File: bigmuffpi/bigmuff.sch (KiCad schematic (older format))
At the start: 62 parts, among them J1 PWR JACK, J2 INPUT, J3 OUTPUT, Q1 BC239, Q2 BC239, Q3 BC239, Q4 BC239, SW1 POWER

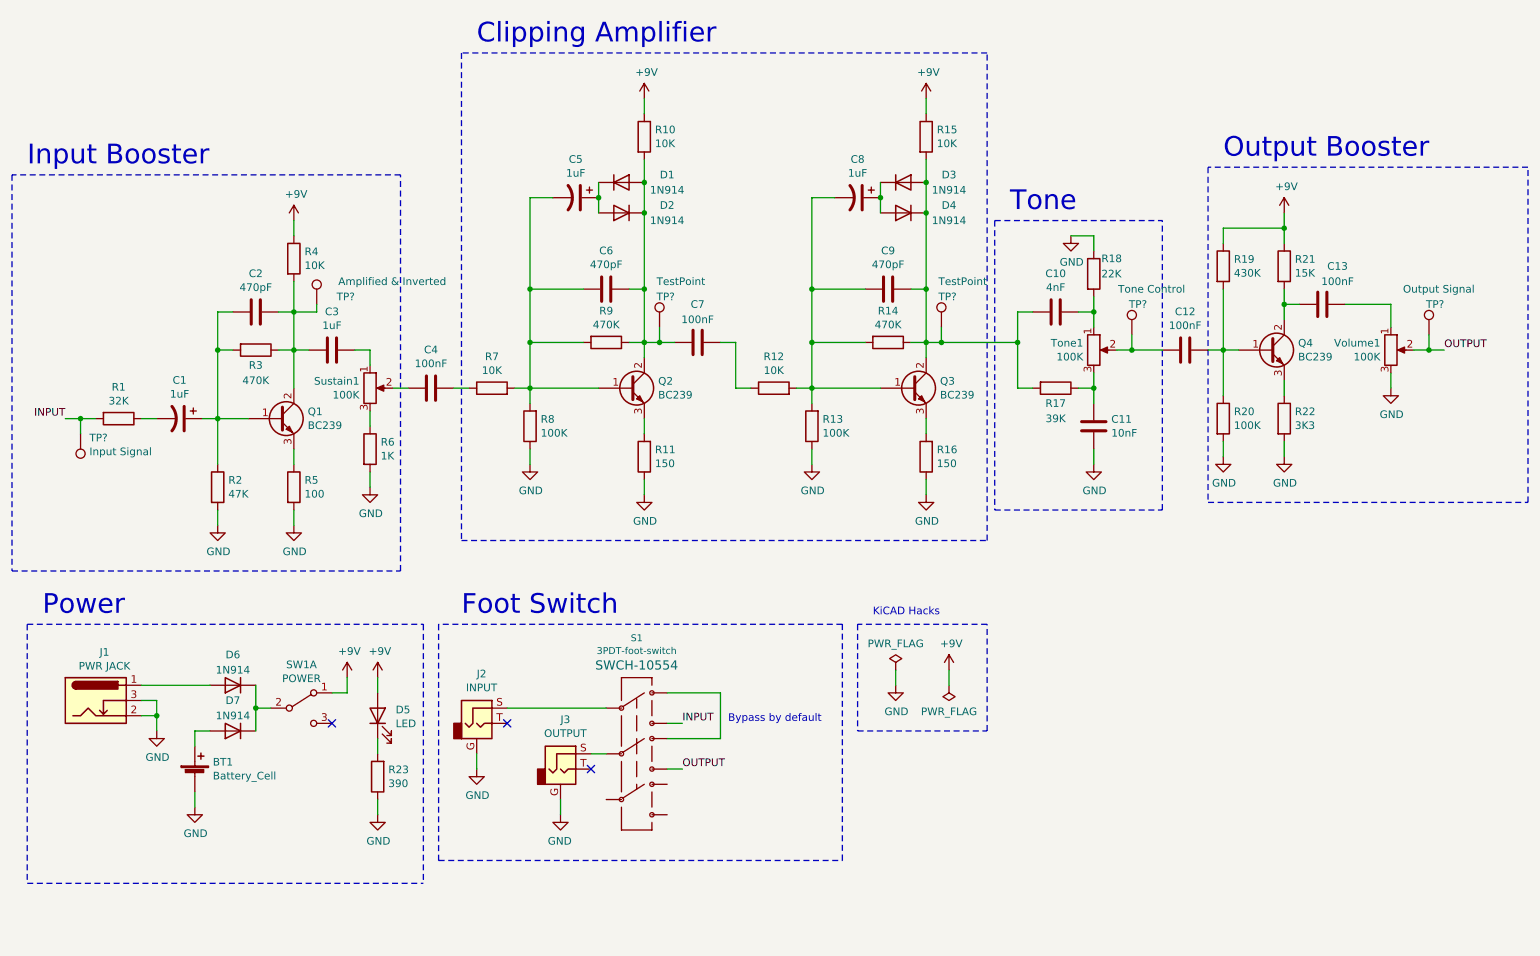
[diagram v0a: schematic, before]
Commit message: add: not connected to switch
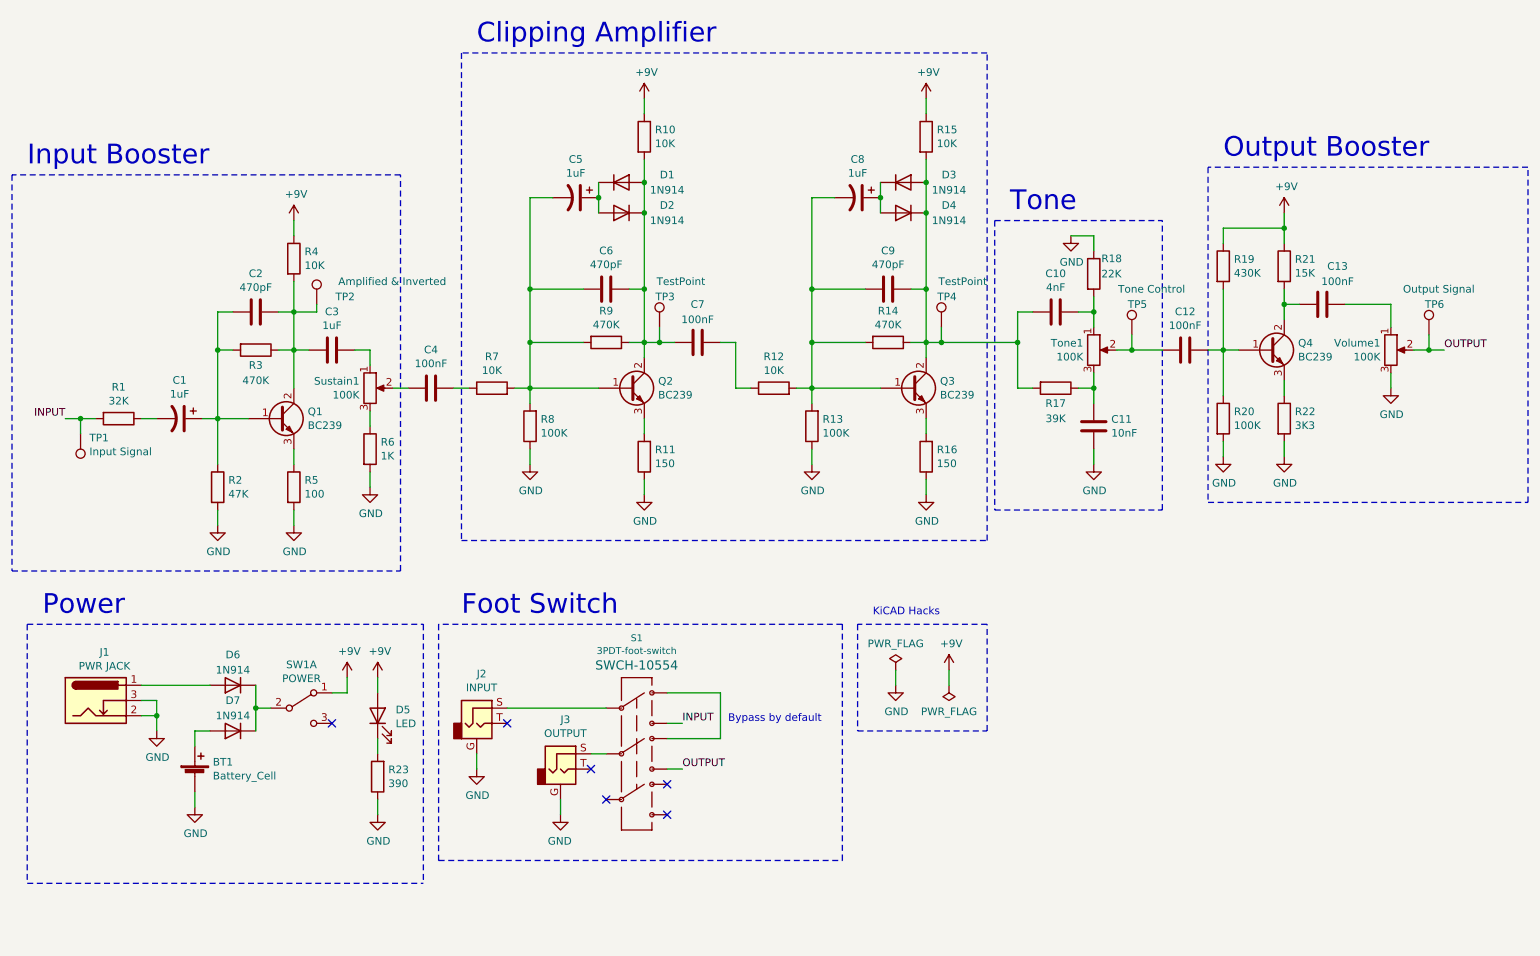
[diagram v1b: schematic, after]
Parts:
- gave numbers to parts that had none: 6
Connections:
- no-connect marks 3 -> 6
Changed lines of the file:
@@
 	1200 5350 3800 5350
 $Comp
-L Connector:TestPoint TP?
+L Connector:TestPoint TP1
 U 1 1 5F1F2FF8
 P 1550 4100
-F 0 "TP?" H 1492 4126 50  0000 R CNN
+F 0 "TP1" H 1492 4126 50  0000 R CNN
 F 1 "Input Signal" H 1492 4217 50  0000 R CNN
 F 2 "" H 1750 4100 50  0001 C CNN
@@
 Connection ~ 1550 4000
 $Comp
-L Connector:TestPoint TP?
+L Connector:TestPoint TP3
 U 1 1 5F208773
 P 5350 3400
-F 0 "TP?" H 5450 3600 50  0000 R CNN
+F 0 "TP3" H 5450 3600 50  0000 R CNN
 F 1 "TestPoint" H 5650 3700 50  0000 R CNN
 F 2 "" H 5550 3400 50  0001 C CNN
@@
 	5350 3500 5450 3500
 $Comp
-L Connector:TestPoint TP?
+L Connector:TestPoint TP4
 U 1 1 5F22B391
 P 7200 3400
-F 0 "TP?" H 7300 3600 50  0000 R CNN
+F 0 "TP4" H 7300 3600 50  0000 R CNN
 F 1 "TestPoint" H 7500 3700 50  0000 R CNN
 F 2 "" H 7400 3400 50  0001 C CNN
@@
 	7200 3500 7700 3500
 $Comp
-L Connector:TestPoint TP?
+L Connector:TestPoint TP6
 U 1 1 5F2380CB
 P 10400 3450
-F 0 "TP?" H 10500 3650 50  0000 R CNN
+F 0 "TP6" H 10500 3650 50  0000 R CNN
 F 1 "Output Signal" H 10700 3750 50  0000 R CNN
 F 2 "" H 10600 3450 50  0001 C CNN
@@
 Connection ~ 10400 3550
 $Comp
-L Connector:TestPoint TP?
+L Connector:TestPoint TP5
 U 1 1 5F24FCF1
 P 8450 3450
-F 0 "TP?" H 8550 3650 50  0000 R CNN
+F 0 "TP5" H 8550 3650 50  0000 R CNN
 F 1 "Tone Control" H 8800 3750 50  0000 R CNN
 F 2 "" H 8650 3450 50  0001 C CNN
@@
 	2950 3300 3100 3300
 $Comp
-L Connector:TestPoint TP?
+L Connector:TestPoint TP2
 U 1 1 5F2936BD
 P 3100 3250
-F 0 "TP?" H 3350 3300 50  0000 R CNN
+F 0 "TP2" H 3350 3300 50  0000 R CNN
 F 1 "Amplified & Inverted" H 3950 3400 50  0000 R CNN
 F 2 "" H 3300 3250 50  0001 C CNN
@@
 	1    0    0    -1
 $EndComp
+NoConn ~ 5400 6400
+NoConn ~ 5400 6600
+NoConn ~ 5000 6500
 $EndSCHEMATC

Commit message: add: assign big bunch of components
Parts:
- C1, C5, C8: Mfr. No (none) -> 860020672005; Mouser (none) -> 710-860020672005
- D1, D2, D3, D4, D6, D7: LCSC (none) -> C125665; Mfr. No (none) -> 1N914; Mouser (none) -> 512-1N914
- D5: LCSC (none) -> C162069; Mfr. No (none) -> TLHR5400-AS12Z; Mouser (none) -> 78-TLHR5400-AS12Z
- J1: LCSC (none) -> C381116; Mfr. No (none) -> DC-005-5A-2.0
- J2, J3: Mfr. No (none) -> NMJ6HC-S; Mouser (none) -> 550-NMJ6HCS
- Q1, Q2, Q3, Q4: Mfr. No (none) -> BC549CTA; Mouser (none) -> 512-BC549CTA
- S1: footprint 3PDT-foot-switch -> (none); Mfr. No (none) -> SF17020F-0302-21R-L-015; Mouser (none) -> 107-SF17020F-32-21RL
- SW1: Mfr. No (none) -> 100SP1T1B1M1QEH; Mouser (none) -> 612-100-A1111
- Sustain1, Tone1, Volume1: Mfr. No (none) -> RK09D113BF25B15; Mouser (none) -> 688-RK09D113BF25B15
- TP1, TP2, TP3, TP4, TP5, TP6: footprint (none) -> TestPoint:TestPoint_Pad_2.0x2.0mm

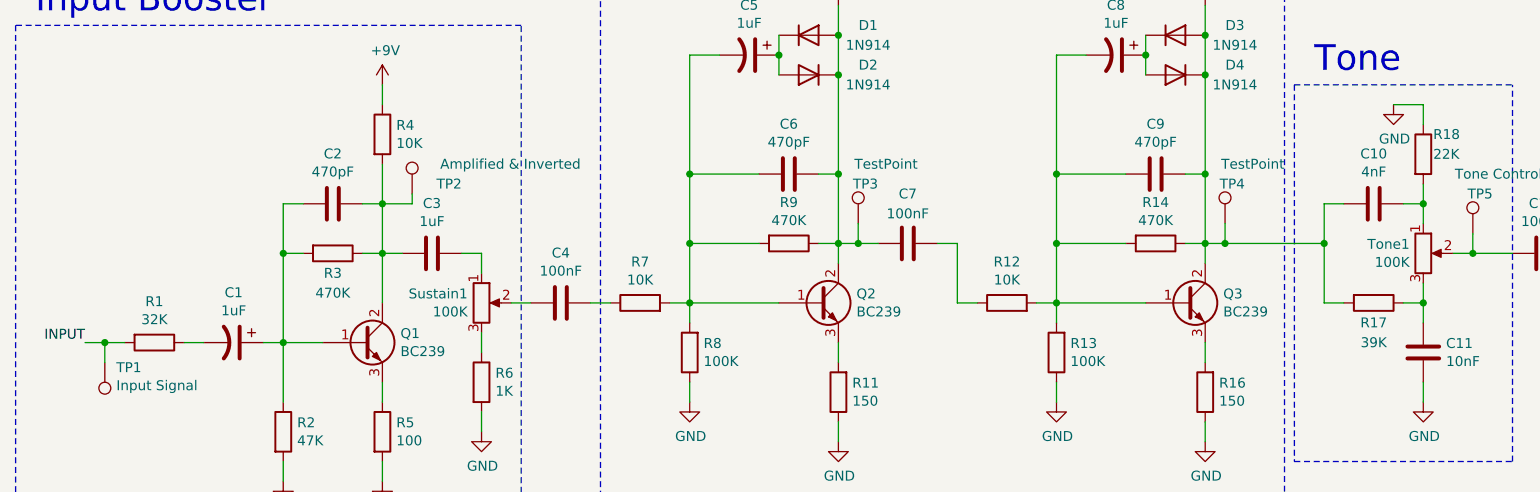
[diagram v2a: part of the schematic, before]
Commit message: fix: audio IN/OUT change to 4 pin jacks
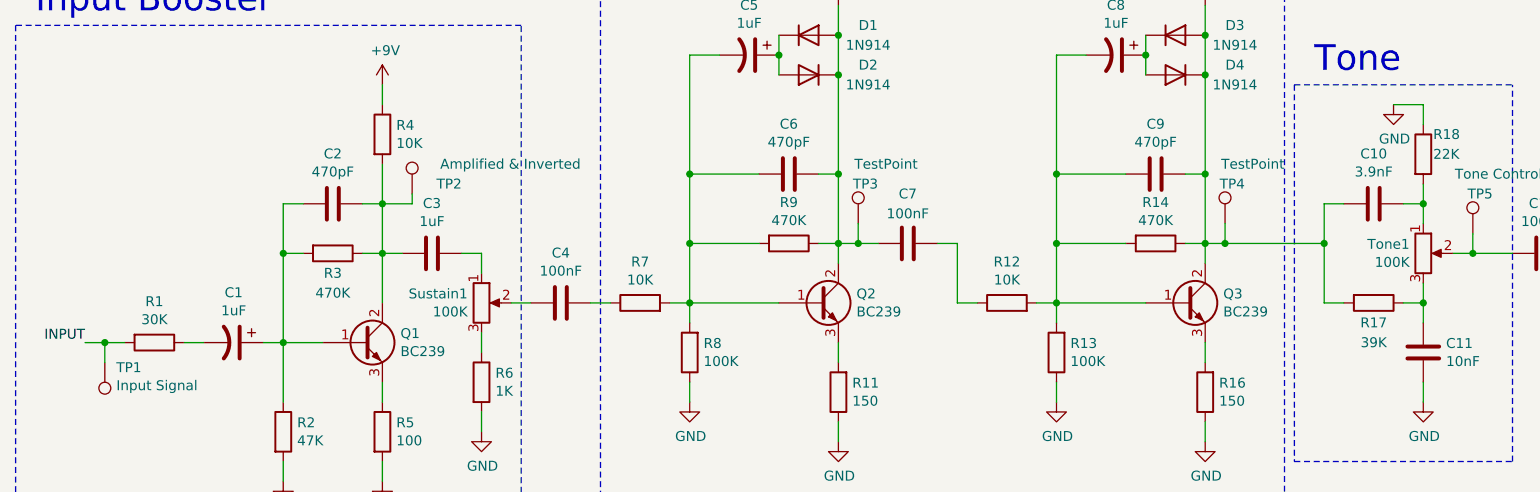
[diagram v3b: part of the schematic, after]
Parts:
- BT1: Mfr. No (none) -> 232; Mouser (none) -> 534-232; Supplier (none) -> Mouser
- C1, C5, C8, D5, Q1, Q2, Q3, Q4, Sustain1, Tone1, Volume1: Supplier (none) -> Mouser
- C10: value 4nF -> 3.9nF; Mfr. No (none) -> K392K15X7RF53L2; Mouser (none) -> 594-K392K15X7RF53L2; Supplier (none) -> Mouser
- C11: Mfr. No (none) -> K103K15X7RH5TH5; Mouser (none) -> 594-K103K15X7RH5TH5; Supplier (none) -> Mouser
- C12, C13, C4, C7: Mfr. No (none) -> K104K15X7RF53H5; Mouser (none) -> 594-K104K15X7RF53H5; Supplier (none) -> Mouser
- C2, C6, C9: Mfr. No (none) -> K471K15X7RF53H5; Mouser (none) -> 594-K471K15X7RF53H5; Supplier (none) -> Mouser
- C3: Mfr. No (none) -> FG28X5R1H105KRT00; Mouser (none) -> 810-FG28X5R1H105KRT0; Supplier (none) -> Mouser
- D1, D2, D3, D4, D6, D7: LCSC C125665 -> C125665; Supplier (none) -> Mouser
- J1: Supplier (none) -> LCSC
- J2, J3: Mfr. No NMJ6HC-S -> NMJ4HC-S; Mouser 550-NMJ6HCS -> 568-NMJ4HC-S; Supplier (none) -> Mouser
- R1: value 32K -> 30K; Mfr. No (none) -> CFR-12JB-52-30K; Mouser (none) -> 603-CFR-12JB-52-30K; Supplier (none) -> Mouser
- R10, R12, R15, R4, R7: Mfr. No (none) -> CFR-12JT-52-10K; Mouser (none) -> 603-CFR-12JT-52-10K; Supplier (none) -> Mouser
- R11, R16: Mfr. No (none) -> CFR-12JT-52-150R; Mouser (none) -> 603-CFR-12JT-52-150R; Supplier (none) -> Mouser
- R13, R20, R8: Mfr. No (none) -> CFR-12JR-52-100K; Mouser (none) -> 603-CFR-12JR-52-100K; Supplier (none) -> Mouser
- R14, R3, R9: Mfr. No (none) -> CFR-12JT-52-470K; Mouser (none) -> 603-CFR-12JT-52-470K; Supplier (none) -> Mouser
- R17: Mfr. No (none) -> CFR-12JR-52-39K; Mouser (none) -> 603-CFR-12JR-52-39K; Supplier (none) -> Mouser
- R18: Mfr. No (none) -> CFR-12JT-52-22K; Mouser (none) -> 603-CFR-12JT-52-22K; Supplier (none) -> Mouser
- R19: Mfr. No (none) -> CFR-12JB-52-430K; Mouser (none) -> 603-CFR-12JB-52-430K; Supplier (none) -> Mouser
- R2: Mfr. No (none) -> CFR-12JB-52-47K; Mouser (none) -> 603-CFR-12JB-52-47K; Supplier (none) -> Mouser
- R21: Mfr. No (none) -> CFR-12JT-52-15K; Mouser (none) -> 603-CFR-12JT-52-15K; Supplier (none) -> Mouser
- R22: Mfr. No (none) -> CFR-12JR-52-3K3; Mouser (none) -> 603-CFR-12JR-52-3K3; Supplier (none) -> Mouser
- R23: Mfr. No (none) -> CFR-12JB-52-390R; Mouser (none) -> 603-CFR-12JB-52-390R; Supplier (none) -> Mouser
- R5: Mfr. No (none) -> CFR-12JT-52-100R; Mouser (none) -> 603-CFR-12JT-52-100R; Supplier (none) -> Mouser
- R6: Mfr. No (none) -> CFR-12JT-52-1K; Mouser (none) -> 603-CFR-12JT-52-1K; Supplier (none) -> Mouser
- S1: Aliexpress (none) -> https://www.aliexpress.com/item/1761081145.html?spm=a2g0o.c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; Comment (none) -> Much much cheaper from Aliexpress (look for 3PDT); Mfr. No SF17020F-0302-21R-L-015 -> 3PDT 9-Pin; Supplier (none) -> Aliexpress
- SW1: LCSC (none) -> C273357; Mfr. No 100SP1T1B1M1QEH -> 100SP3T2B4M6RE; Supplier (none) -> LCSC

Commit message: add: mostly hw layout
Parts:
- removed J2: INPUT, symbol Connector:AudioJack2_Ground
- removed J3: OUTPUT, symbol Connector:AudioJack2_Ground
- added J4: OUTPUT, bigmuffpi:NMJ6HC-S, symbol Connector:AudioJack2
- added J5: INPUT, bigmuffpi:NMJ6HC-S, symbol Connector:AudioJack2
- BT1: footprint (none) -> LED_THT:LED_D5.0mm; Mfr. No 232 -> 79; Mouser 534-232 -> 534-079
- C1, C5, C8: footprint Capacitor_THT:C_Disc_D5.0mm_W2.5mm_P5.00mm -> Capacitor_THT:CP_Radial_D5.0mm_P2.00mm
- C10, C11, C12, C13, C2, C3, C4, C6, C7, C9: footprint Capacitor_THT:C_Disc_D5.0mm_W2.5mm_P5.00mm -> Capacitor_THT:C_Disc_D4.7mm_W2.5mm_P5.00mm
- J1: footprint (none) -> Connector_PinHeader_2.54mm:PinHeader_1x03_P2.54mm_Vertical; LCSC C381116 -> (none); Mfr. No DC-005-5A-2.0 -> (none); Supplier LCSC -> Aliexpress
- S1: footprint (none) -> bigmuffpi:SF17020F-0302-21R-L
- SW1: footprint (none) -> bigmuffpi:E-SWITCH-100SP3T2B4M6RE
- Sustain1, Tone1, Volume1: footprint (none) -> Potentiometer_THT:Potentiometer_Alps_RK09K_Single_Vertical
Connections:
- net GND: now also J4.S, J5.S
- net at S1.2: now also J5.T
- net at S1.5: now also J4.T
- no-connect marks 6 -> 4
